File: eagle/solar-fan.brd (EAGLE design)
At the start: 100 x 80 mm, 36 parts, among them J1 POWER_JACKPTH, J2 USB-A-S, J3 7805, U1 LT3652, U2 ATTINY85

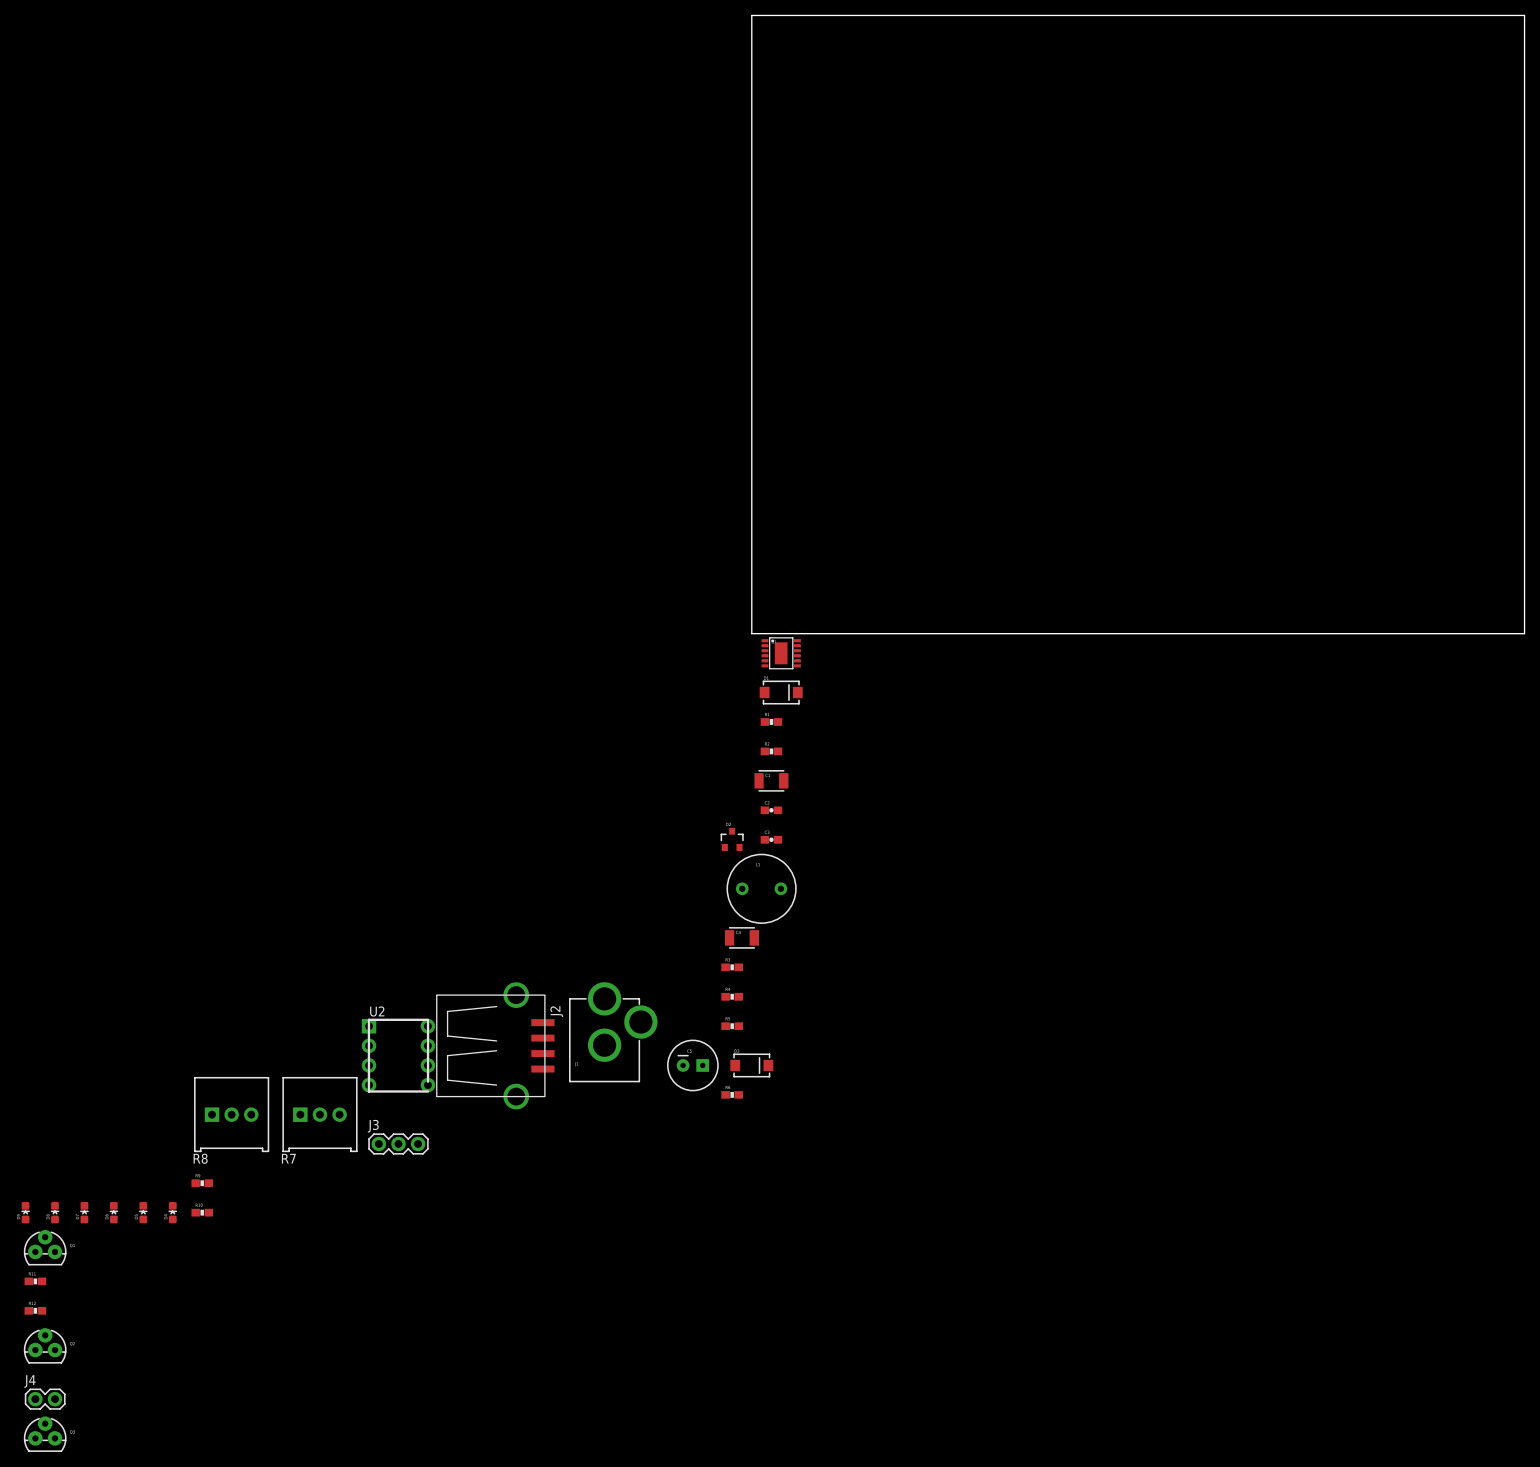
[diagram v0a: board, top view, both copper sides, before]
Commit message: first draft of board layout, minor schematic fixes
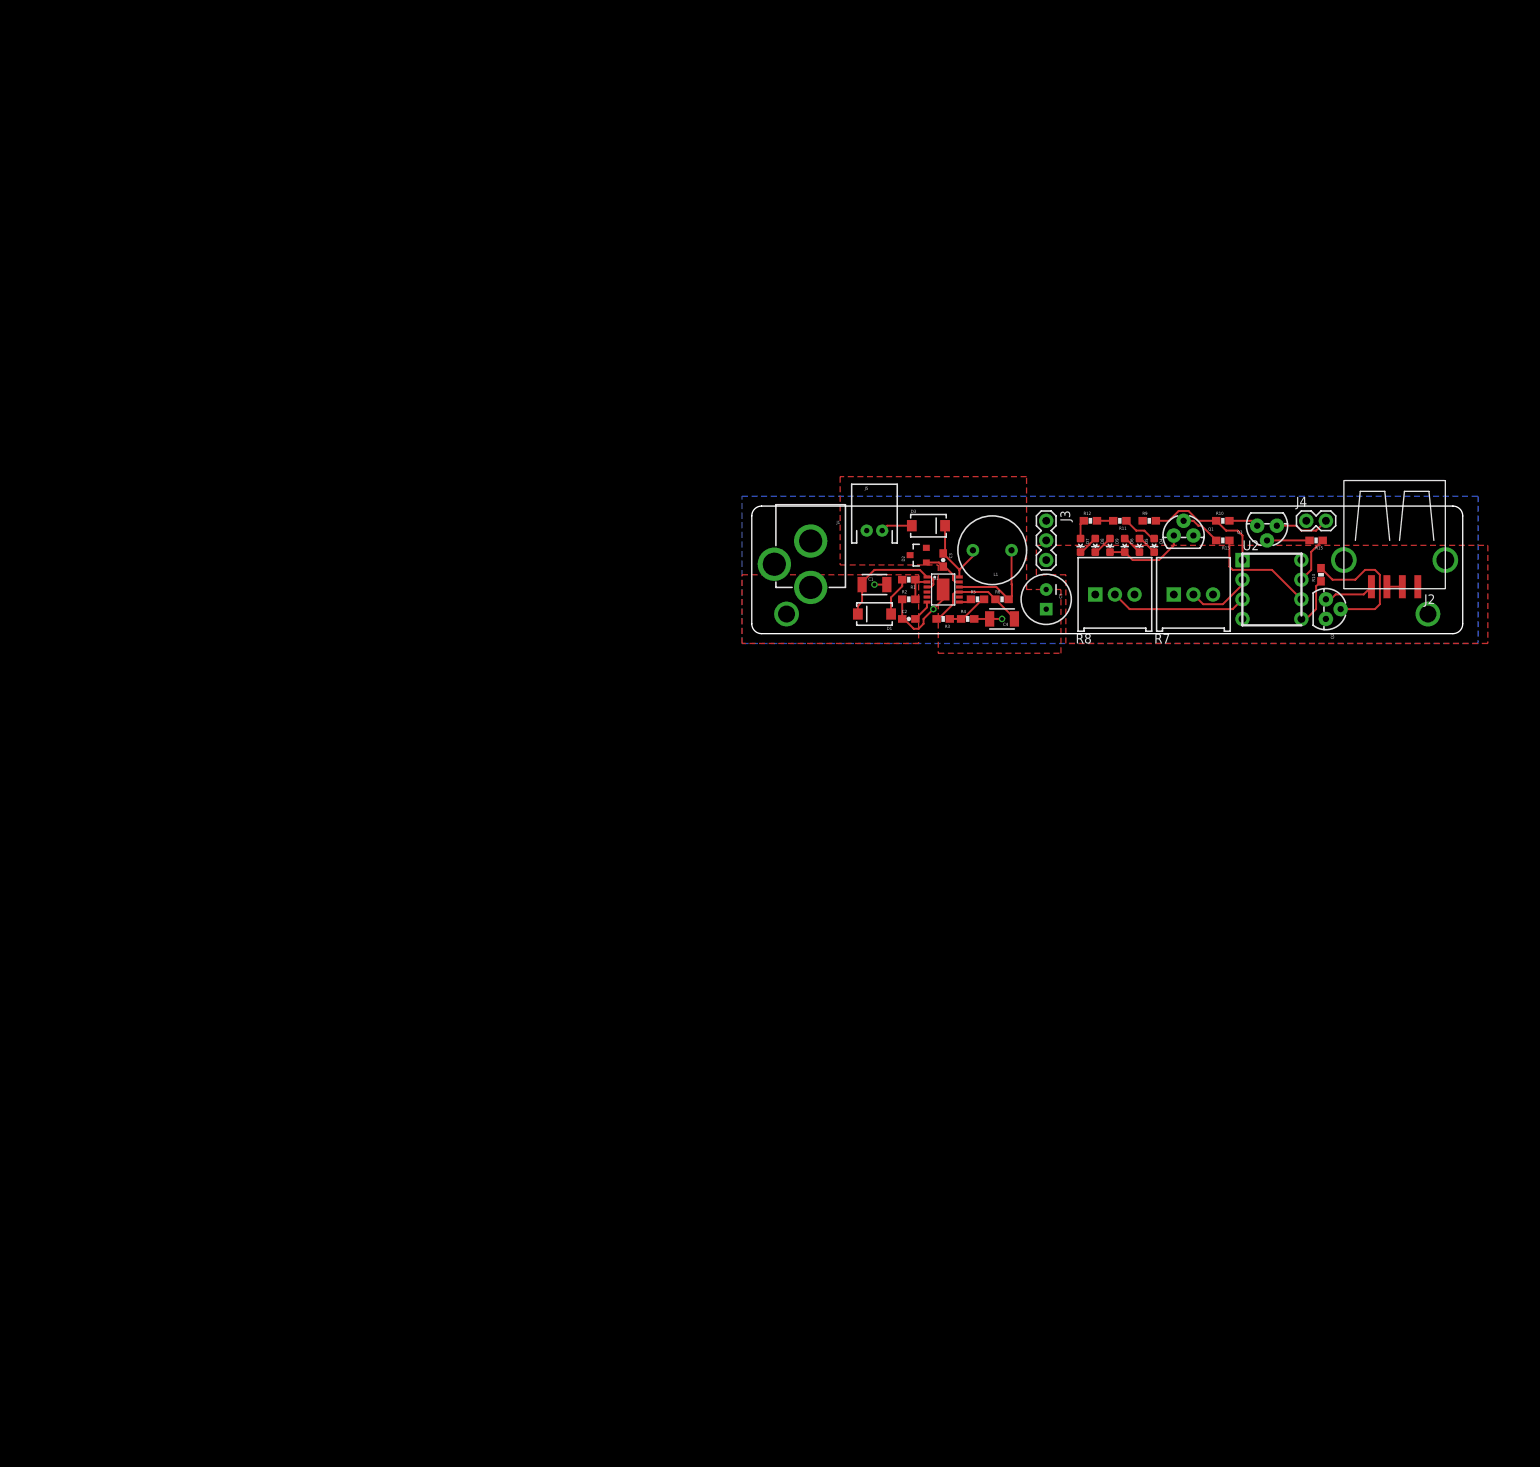
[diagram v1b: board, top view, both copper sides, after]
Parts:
- added J5: (no value), SparkFun-Connectors:JST-2-PTH
- added R13, R14, R15: 100k, SparkFun-Passives:0603-RES
- moved J4 199.9 mm to (71.8, 14.6)
- moved Q3 197.4 mm to (66.7, 14.0), turned to 180 degrees
- moved Q2 191.5 mm to (74.3, 3.17), turned to 270 degrees
- moved Q1 174.1 mm to (55.9, 12.7)
- moved R11 171.4 mm to (47.6, 14.6), turned to 180 degrees
- moved R12 170.6 mm to (43.8, 14.6)
- moved D9 164.8 mm to (46.4, 11.4), turned to 180 degrees
- moved D8 159.9 mm to (44.5, 11.4), turned to 180 degrees
- moved R10 159.6 mm to (61.0, 14.6)
- moved D6 156.7 mm to (48.3, 11.4), turned to 180 degrees
- moved D5 155.2 mm to (50.2, 11.4), turned to 180 degrees
- moved D7 155.2 mm to (42.5, 11.4), turned to 180 degrees
- moved D4 153.6 mm to (52.1, 11.4), turned to 180 degrees
- moved R9 149.6 mm to (51.4, 14.6)
- moved R8 132.6 mm to (47.0, 5.08)
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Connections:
- removed net N$10: C5.1
- new net N$1: Q1.2, R13.2
- new net N$2: Q2.2, R14.2
- new net N$3: Q3.2, R15.2
- net FAN_OUT: now also R15.1, U2.7; no longer Q3.2, U2.5
- net GND: now also J5.2
- net LED_OUT: now also R13.1; no longer Q1.2
- net USB_OUT: now also R14.1, U2.5; no longer Q2.2, U2.7
- net V_BATT: now also C5.1, J5.1
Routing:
- net GND: track 0.00 -> 24.9 mm, vias 0 -> 3
- net N$2: track 0.00 -> 18.2 mm
- net LED_IN: track 0.00 -> 17.8 mm
- net SHDN: track 0.00 -> 16.3 mm
- net VBAT: track 0.00 -> 16.2 mm
- net V_BATT: track 0.00 -> 15.9 mm
- net LED_OUT: track 0.00 -> 14.5 mm
- net SENSE: track 0.00 -> 13.6 mm
- net SW: track 0.00 -> 10.8 mm
- net N$19: track 0.00 -> 10.7 mm
- net FAN_IN: track 0.00 -> 8.56 mm
- net N$22: track 0.00 -> 7.14 mm
- net N$21: track 0.00 -> 6.57 mm
- net USB_OUT: track 0.00 -> 6.29 mm
- net FAN_OUT: track 0.00 -> 6.22 mm
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- added copper zone on layer 1, net 5V
- added copper zone on layer 16, net GND
- added copper zone on layer 1, net VIN
- added copper zone on layer 1, net V_BATT
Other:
- board size 100 x 80 mm -> 92 x 16.5 mm

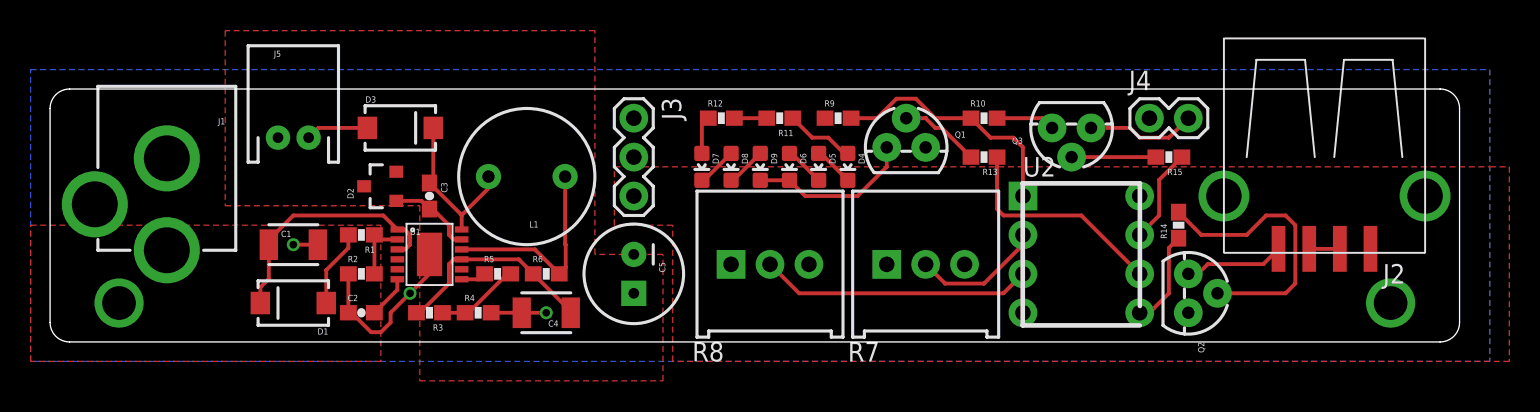
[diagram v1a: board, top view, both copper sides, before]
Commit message: minor layout updates, adding PNs to schematic
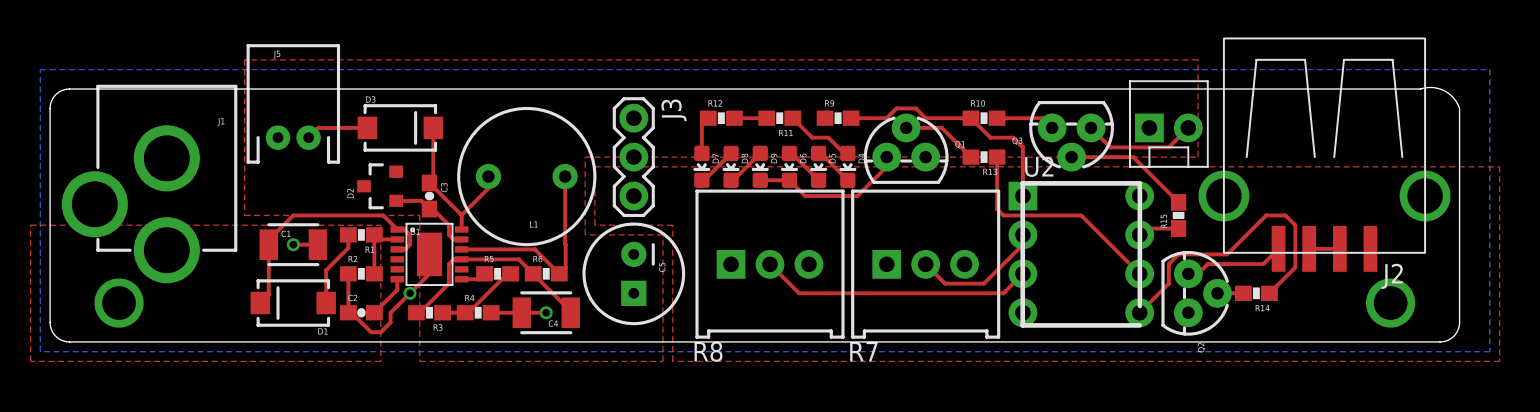
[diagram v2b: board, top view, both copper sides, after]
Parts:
- J4: device SparkFun-Connectors:1X02 -> SparkFun-Connectors:MOLEX-1X2
- moved R14 6.75 mm to (78.7, 3.17), turned to 180 degrees
- moved R15 3.86 mm to (73.7, 8.26), turned to 90 degrees
- moved J4 0.63 mm to (71.8, 14.0)
- moved Q1 0.63 mm to (55.9, 12.1)
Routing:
- net N$2: track 18.2 -> 1.69 mm
- net USB_OUT: track 6.29 -> 18.9 mm
- net FAN_OUT: track 6.22 -> 2.71 mm
- net N$3: track 5.50 -> 8.21 mm
- net N$19: track 10.7 -> 10.1 mm
- net VBAT: track 16.2 -> 15.7 mm
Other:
- board size 92 x 16.5 mm -> 92 x 16.6 mm

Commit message: layout update, bom, components
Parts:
- removed J2: USB-A-S, SparkFun-Connectors:USB-A-S
- added C6: 0.1uf, SparkFun-Passives:0603-CAP
- added C7: 0.33uf, SparkFun-Passives:0603-CAP
- added J6: USB_, SparkFun-Connectors:USB-A-S-SILK-FEMALE
- moved D9 5.24 mm to (47.6, 16.5), turned to 270 degrees
- moved D7 5.24 mm to (43.8, 16.5), turned to 90 degrees
- moved D4 5.12 mm to (51.4, 16.5), turned to 270 degrees
- moved J4 3.86 mm to (71.1, 17.8)
- moved Q3 3.86 mm to (66.0, 17.8)
- moved J1 3.81 mm to (7.62, 23.5)
- moved C1 3.81 mm to (15.9, 10.2)
- moved C3 3.81 mm to (24.8, 13.3)
- moved C5 3.81 mm to (38.1, 8.26)
- moved D2 3.81 mm to (21.6, 14.0)
- moved D3 3.81 mm to (22.9, 17.8)
- moved L1 3.81 mm to (31.1, 14.6)
- moved Q1 3.81 mm to (55.9, 15.9)
- moved Q2 3.81 mm to (74.3, 6.99)
- moved R13 3.81 mm to (61.0, 15.9)
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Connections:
- removed net N$22: J4.2, Q3.1
- new net N$6: J4.1, Q3.1
- net 5V: now also C6.1, J6.VBUS; no longer J2.VBUS
- net GND: now also C6.2, C7.2, J5.1; no longer J5.2
- net N$20: now also J6.D+, J6.D-; no longer J2.D+, J2.D-
- net N$21: now also J6.GND; no longer J2.GND
- net V_BATT: now also C7.1, J4.2, J5.2; no longer J4.1, J5.1
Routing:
- net V_BATT: track 15.9 -> 0.21 mm
- net N$22: track 7.40 -> 0.00 mm
- net N$6: track 0.00 -> 3.81 mm
- net N$19: track 10.1 -> 12.4 mm
- net GND: track 24.9 -> 26.8 mm, vias 3 -> 4
- net N$13: track 4.55 -> 2.87 mm
- net N$2: track 1.69 -> 2.59 mm
- net N$21: track 6.57 -> 5.82 mm
- net N$15: track 2.63 -> 1.91 mm
- net N$16: track 2.63 -> 1.91 mm
- net N$3: track 8.21 -> 8.85 mm
- net N$17: track 2.63 -> 2.06 mm
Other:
- board size 92 x 16.6 mm -> 92 x 19.7 mm

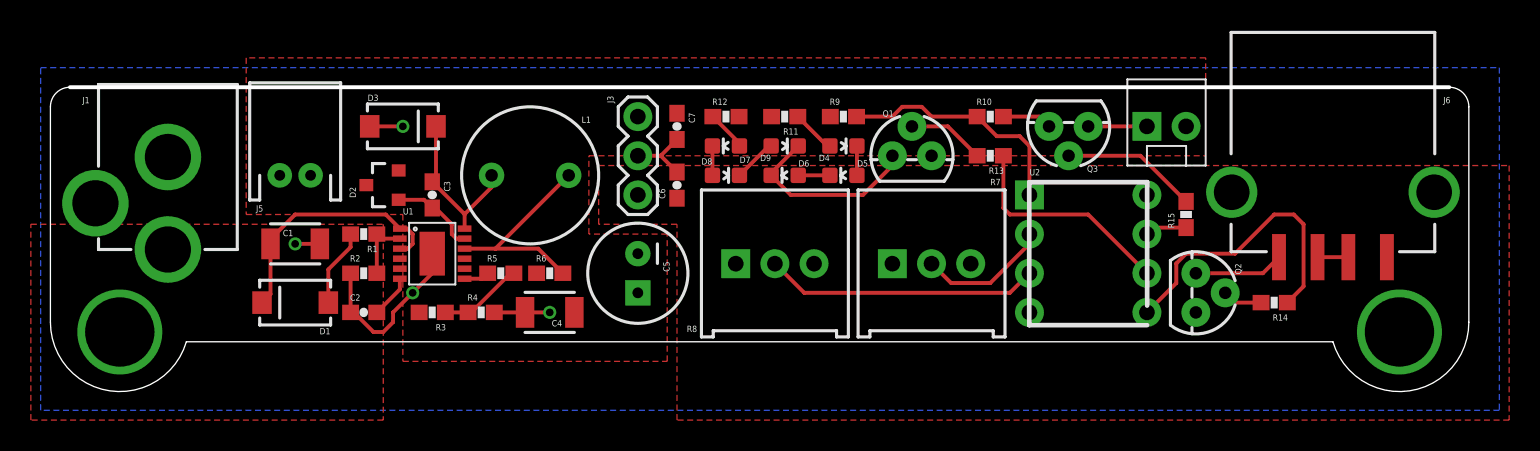
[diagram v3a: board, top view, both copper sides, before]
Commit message: updated fan connector and layout, silk screen, mfg files
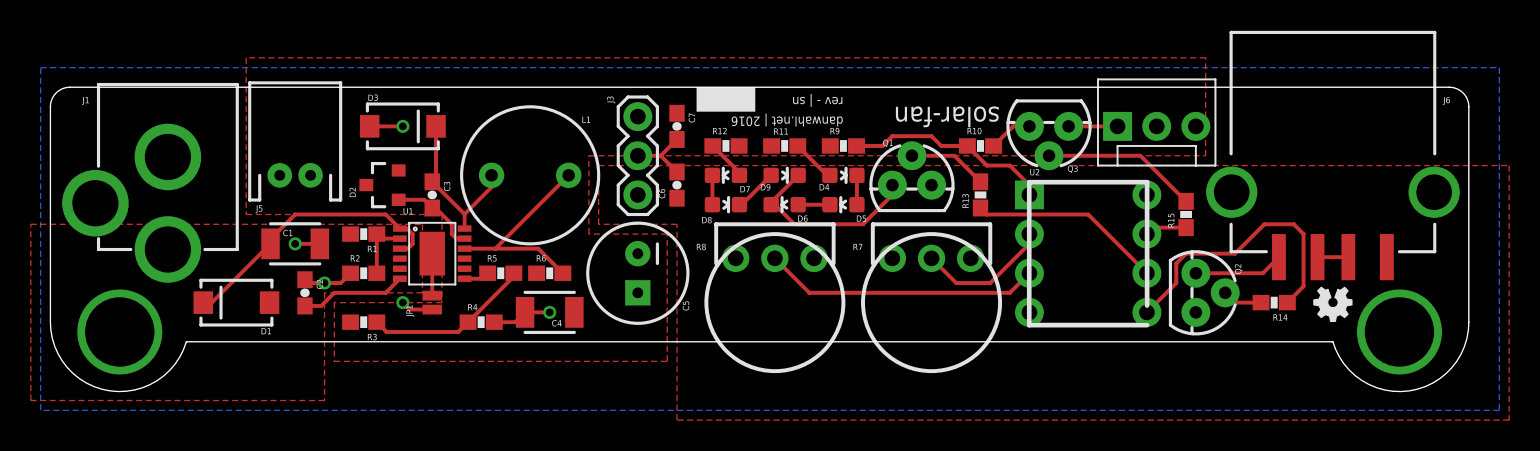
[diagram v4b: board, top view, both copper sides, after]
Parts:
- removed J4: (no value), SparkFun-Connectors:MOLEX-1X2
- added J2: (no value), SparkFun-Connectors:MOLEX-1X3
- added JP1: JUMPER-PAD-2-NO, SparkFun-Passives:PAD-JUMPER-2-NO_NO_SILK
- added LOGO1: OSHW-LOGOMINI, SparkFun-Aesthetics:OSHW-LOGO-MINI
- R7, R8: value TSR-3386 -> 3352T; device SparkFun-Electromechanical:3386U -> bourns3352:3352T
- moved R3 4.49 mm to (20.3, 5.08)
- moved C2 4.02 mm to (16.5, 6.99), turned to 270 degrees
- moved D1 3.81 mm to (12.1, 6.35)
- moved R13 2.62 mm to (60.3, 13.3), turned to 90 degrees
- moved R7 2.54 mm to (57.1, 6.35), turned to 180 degrees
- moved R8 2.54 mm to (47.0, 6.35), turned to 180 degrees
- moved R10 2.01 mm to (60.3, 16.5)
- moved D4 1.91 mm to (51.4, 14.6)
- moved D5 1.91 mm to (51.4, 12.7)
- moved D6 1.91 mm to (47.6, 12.7)
- moved D7 1.91 mm to (43.8, 14.6)
- moved D8 1.91 mm to (43.8, 12.7)
- moved D9 1.91 mm to (47.6, 14.6)
- moved Q1 1.90 mm to (55.9, 14.0)
- moved R11 1.90 mm to (47.6, 16.5)
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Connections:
- new net PAD: JP1.2, U1.13
- net 5V: now also R7.CCW, R8.CCW; no longer R7.1, R8.1
- net FAN_IN: now also R7.WIPER; no longer R7.2
- net GND: now also JP1.1, R7.CW, R8.CW; no longer R7.3, R8.3, U1.13
- net LED_IN: now also R8.WIPER; no longer R8.2
- net N$6: now also J2.1; no longer J4.1
- net V_BATT: now also J2.2; no longer J4.2
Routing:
- net GND: track 26.8 -> 20.3 mm, vias 4 -> 5
- net N$7: track 5.50 -> 11.1 mm
- net VIN: track 5.04 -> 0.00 mm
- net TIMER: track 2.80 -> 6.89 mm
- net PAD: track 0.00 -> 2.73 mm
- net VBAT: track 15.7 -> 13.4 mm
- net LED_OUT: track 14.5 -> 12.5 mm
- net SHDN: track 16.3 -> 18.2 mm
- net N$3: track 8.85 -> 10.1 mm
- net USB_OUT: track 19.3 -> 18.4 mm
- net N$6: track 3.81 -> 3.17 mm
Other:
- board text added: "danwahl.net | 2016"
- board text added: "rev - | sn"
- board text added: "solar-fan"
